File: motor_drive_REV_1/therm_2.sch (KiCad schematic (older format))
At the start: 3 parts, among them J7 Conn_01x02

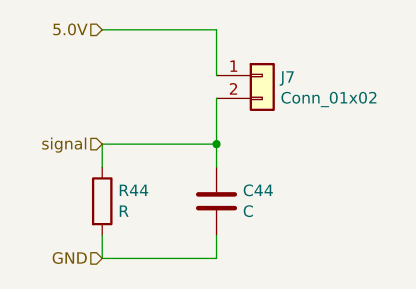
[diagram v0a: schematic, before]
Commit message: gate drive rework and schematic re-organization
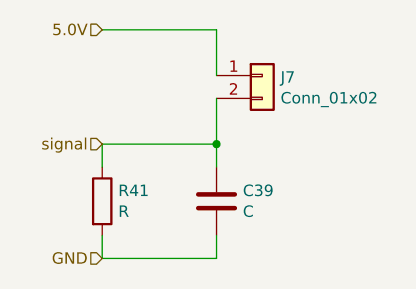
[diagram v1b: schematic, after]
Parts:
- renumbered C44 to C39, R44 to R41
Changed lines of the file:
@@
 $Descr A4 11693 8268
 encoding utf-8
-Sheet 16 16
+Sheet 16 7
 Title ""
 Date ""
@@
 P 5150 3550
 AR Path="/5E41A78C/5E41E7F8" Ref="R?"  Part="1"
-AR Path="/5E41D6EC/5E41E7F8" Ref="R44"  Part="1"
-F 0 "R44" H 5220 3596 50  0000 L CNN
+AR Path="/5E41D6EC/5E41E7F8" Ref="R41"  Part="1"
+F 0 "R41" H 5220 3596 50  0000 L CNN
 F 1 "R" H 5220 3505 50  0000 L CNN
 F 2 "motor_drive_footprints:C_0603_1608Metric" V 5080 3550 50  0001 C CNN
@@
 P 5650 3550
 AR Path="/5E41A78C/5E41E7FE" Ref="C?"  Part="1"
-AR Path="/5E41D6EC/5E41E7FE" Ref="C44"  Part="1"
-F 0 "C44" H 5765 3596 50  0000 L CNN
+AR Path="/5E41D6EC/5E41E7FE" Ref="C39"  Part="1"
+F 0 "C39" H 5765 3596 50  0000 L CNN
 F 1 "C" H 5765 3505 50  0000 L CNN
 F 2 "motor_drive_footprints:C_0603_1608Metric" H 5688 3400 50  0001 C CNN
